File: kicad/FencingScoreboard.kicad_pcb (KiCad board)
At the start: 2 copper layers, 117.5 x 49.5 mm, 20 parts, among them IC1 PIC16F18855-I-ML, IC2 STP16CPC26, IC3 STP16CPC26, J1 USB_B_Micro, J2 Conn_01x03_Pin, J3 Conn_01x03_Pin, Q1 2N7002

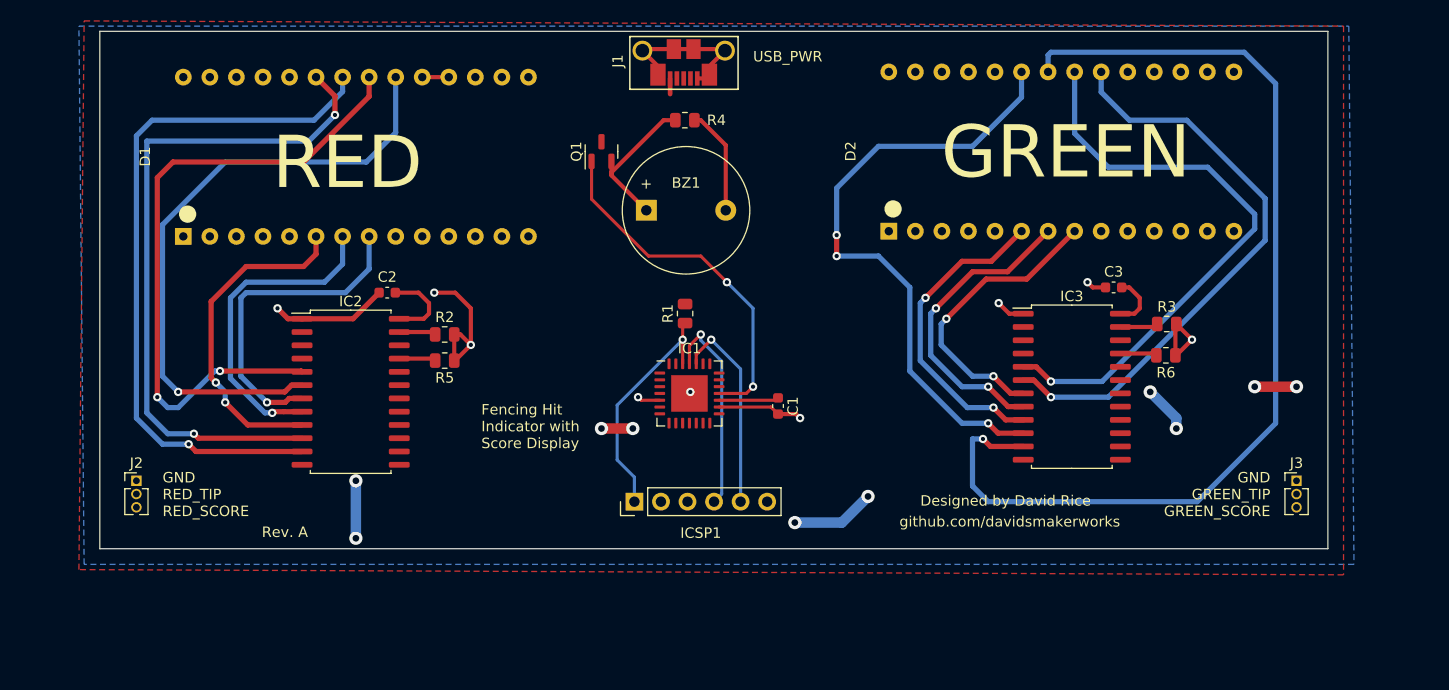
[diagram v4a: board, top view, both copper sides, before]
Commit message: Re-route PCB, update toolchain and device pack
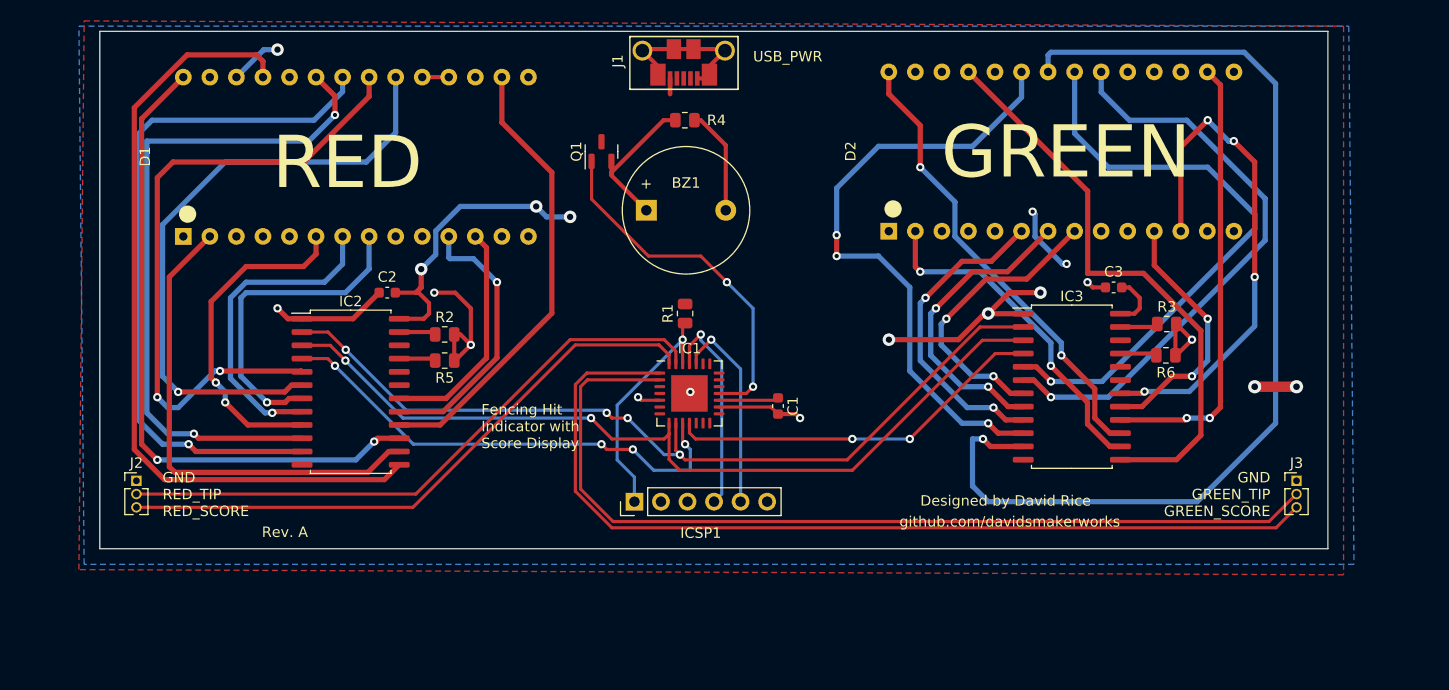
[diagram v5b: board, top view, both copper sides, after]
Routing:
- net GSC: track 0.00 -> 90.0 mm
- net GTIP: track 0.00 -> 88.5 mm
- net LED_DAT: track 0.00 -> 82.5 mm, vias 0 -> 4
- net LED_CLK: track 0.00 -> 82.0 mm, vias 0 -> 2
- net R_OUT8: track 0.00 -> 76.0 mm
- net R_OUT10: track 0.00 -> 63.2 mm, vias 0 -> 2
- net RTIP: track 0.00 -> 59.4 mm
- net RSC: track 0.00 -> 58.6 mm
- net G_OUT8: track 0.00 -> 55.8 mm
- net G_OUT13: track 0.00 -> 49.1 mm, vias 0 -> 4
- net R_OUT9: track 0.00 -> 46.7 mm
- net RED_LE: track 0.00 -> 46.4 mm, vias 0 -> 4
- net G_OUT10: track 0.00 -> 44.3 mm, vias 0 -> 2
- net R_OUT11: track 0.00 -> 43.6 mm
- net G_OUT11: track 0.00 -> 42.7 mm, vias 0 -> 2
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
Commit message: Implement new LED driver code and active buzzer, other minor updates
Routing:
- net +5V: track 55.2 -> 56.3 mm, vias 6 -> 7
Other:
- board text added: "Install R4 for piezo buzzer Omit R4 for speaker"
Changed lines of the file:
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@@
+    (effects (font (size 1 1) (thickness 0.15)) (justify left bottom))
+  )
+  (gr_text "Install R4 for\npiezo buzzer\nOmit R4\nfor speaker" (at 151.25 83.75) (layer "F.SilkS")
     (effects (font (size 1 1) (thickness 0.15)) (justify left bottom))
   )
@@
   (segment (start 120.25 98) (end 119.75 98.5) (width 0.5) (layer "F.Cu") (net 3))
   (via (at 134.5 91.25) (size 1.2) (drill 0.6) (layers "F.Cu" "B.Cu") (net 3))
-  (via (at 182 95.75) (size 0.8) (drill 0.4) (layers "F.Cu" "B.Cu") (net 3))
-  (via (at 178.75 90.75) (size 0.8) (drill 0.4) (layers "F.Cu" "B.Cu") (free) (net 3))
+  (via (at 182 95.75) (size 1.2) (drill 0.6) (layers "F.Cu" "B.Cu") (net 3))
+  (via (at 178.75 90.75) (size 1.2) (drill 0.6) (layers "F.Cu" "B.Cu") (free) (net 3))
   (via (at 106.5 75.25) (size 1.2) (drill 0.6) (layers "F.Cu" "B.Cu") (net 3))
+  (via (at 134.75 99.75) (size 1.2) (drill 0.6) (layers "F.Cu" "B.Cu") (net 3))
   (via (at 131.25 90.25) (size 1.2) (drill 0.6) (layers "F.Cu" "B.Cu") (free) (net 3))
   (via (at 120.25 96.25) (size 1.2) (drill 0.6) (layers "F.Cu" "B.Cu") (net 3))
   (segment (start 182 95.75) (end 181.592233 95.75) (width 0.5) (layer "B.Cu") (net 3))
-  (segment (start 131.25 90.25) (end 123.992233 90.25) (width 0.5) (layer "B.Cu") (net 3))
+  (segment (start 124.25 96.25) (end 127.75 99.75) (width 0.5) (layer "B.Cu") (net 3))
   (segment (start 181.592233 95.75) (end 178.98 93.137767) (width 0.5) (layer "B.Cu") (net 3))
+  (segment (start 120.25 96.25) (end 124.25 96.25) (width 0.5) (layer "B.Cu") (net 3))
+  (segment (start 127.75 99.75) (end 134.75 99.75) (width 0.5) (layer "B.Cu") (net 3))
   (segment (start 134.5 91.25) (end 132.25 91.25) (width 0.5) (layer "B.Cu") (net 3))
   (segment (start 105.2 75.25) (end 106.5 75.25) (width 0.5) (layer "B.Cu") (net 3))
   (segment (start 102.57 77.88) (end 105.2 75.25) (width 0.5) (layer "B.Cu") (net 3))
   (segment (start 132.25 91.25) (end 131.25 90.25) (width 0.5) (layer "B.Cu") (net 3))
-  (segment (start 121.64 92.602233) (end 121.64 94.86) (width 0.5) (layer "B.Cu") (net 3))
   (segment (start 178.98 90.98) (end 178.75 90.75) (width 0.5) (layer "B.Cu") (net 3))
-  (segment (start 123.992233 90.25) (end 121.64 92.602233) (width 0.5) (layer "B.Cu") (net 3))
-  (segment (start 121.64 94.86) (end 120.25 96.25) (width 0.5) (layer "B.Cu") (net 3))
   (segment (start 178.98 93.137767) (end 178.98 90.98) (width 0.5) (layer "B.Cu") (net 3))
   (segment (start 96.15 115.152082) (end 96.15 97) (width 0.5) (layer "F.Cu") (net 5))

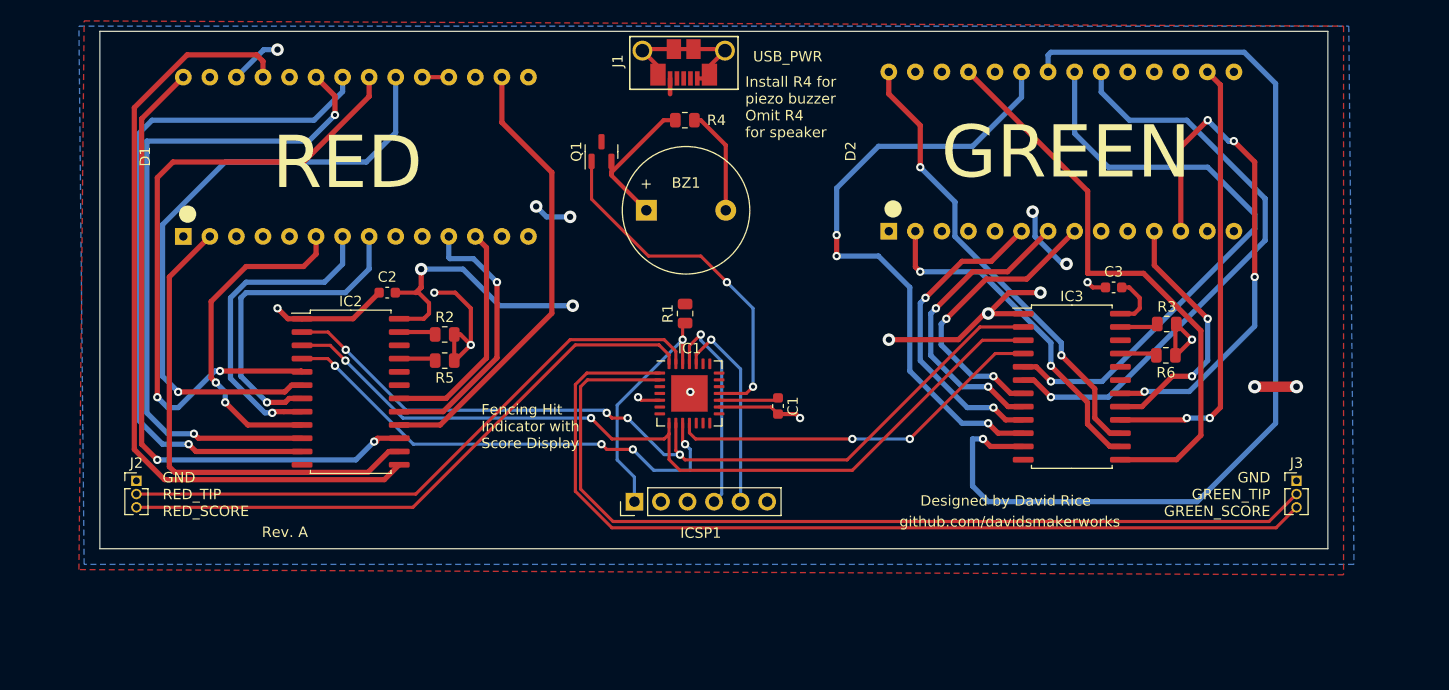
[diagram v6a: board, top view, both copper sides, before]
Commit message: Update J2, J3, BZ1 footprints
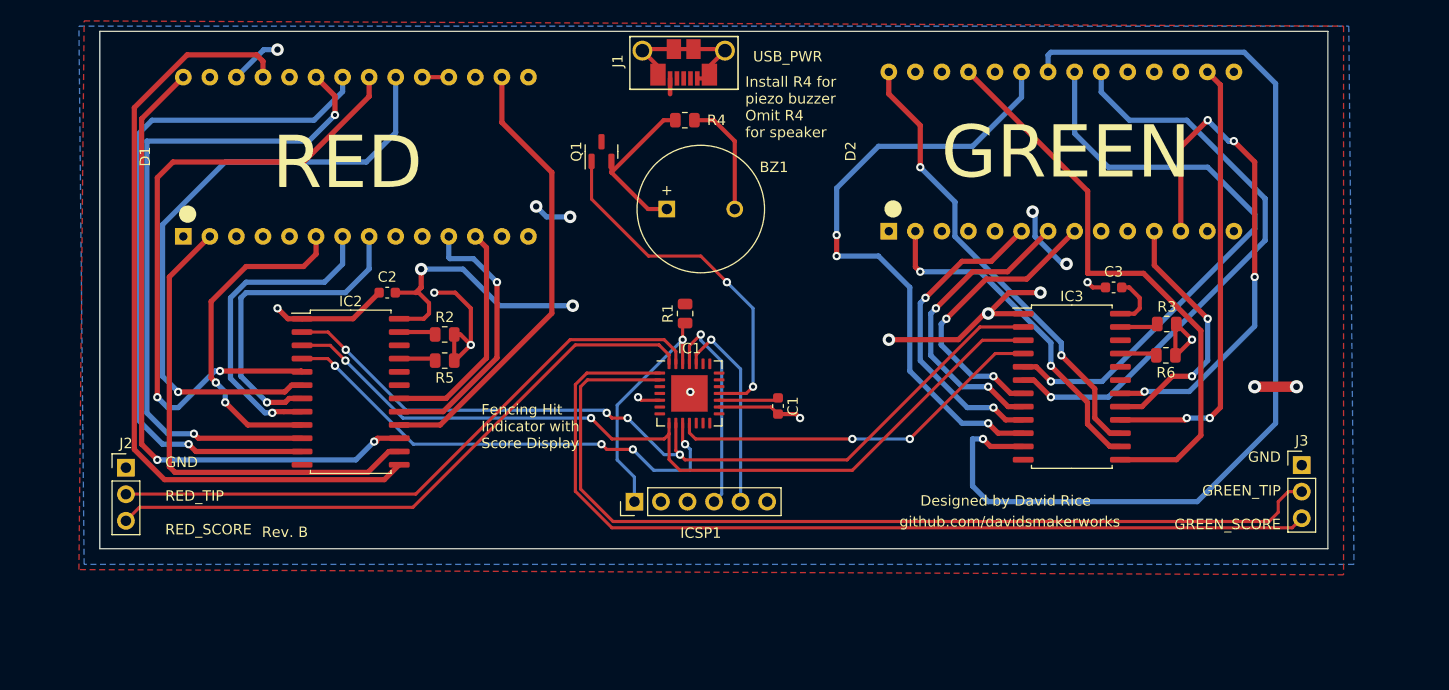
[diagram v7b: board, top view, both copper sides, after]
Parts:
- BZ1: footprint Buzzer_Beeper:Buzzer_12x9.5RM7.6 -> Buzzer_Beeper:MagneticBuzzer_ProSignal_ABT-410-RC
- J2, J3: footprint Connector_PinHeader_1.27mm:PinHeader_1x03_P1.27mm_Vertical -> Connector_PinHeader_2.54mm:PinHeader_1x03_P2.54mm_Vertical
- moved BZ1 1.96 mm to (143.8, 90.5)
- moved J2 1.60 mm to (92.0, 115.2)
- moved J3 1.58 mm to (204.5, 115.0)
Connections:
- IC1 pad 29: GND -> (no net)
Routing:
- net Net-(BZ1--): track 14.3 -> 16.0 mm
- net RSC: track 58.6 -> 60.2 mm
- net GTIP: track 88.5 -> 89.7 mm
- net RTIP: track 59.4 -> 60.4 mm
- net GND: track 94.3 -> 95.3 mm
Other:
- board text added: "Rev. B"
- board text removed: "Rev. A"
